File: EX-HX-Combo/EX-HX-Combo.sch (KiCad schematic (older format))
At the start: 39 parts, among them CN1 DB9 Male, J1 IDE_CONNECTOR, J200 Bus_Tandy_Plus_Through, J3 Bus_Tandy_Plus, SW1 SW_DIP_x10, U1 BIOS FLASH, U2 74HCT245, U3 1.8432 MHz, U4 DS1315, U5 AS6C4008-55PCN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

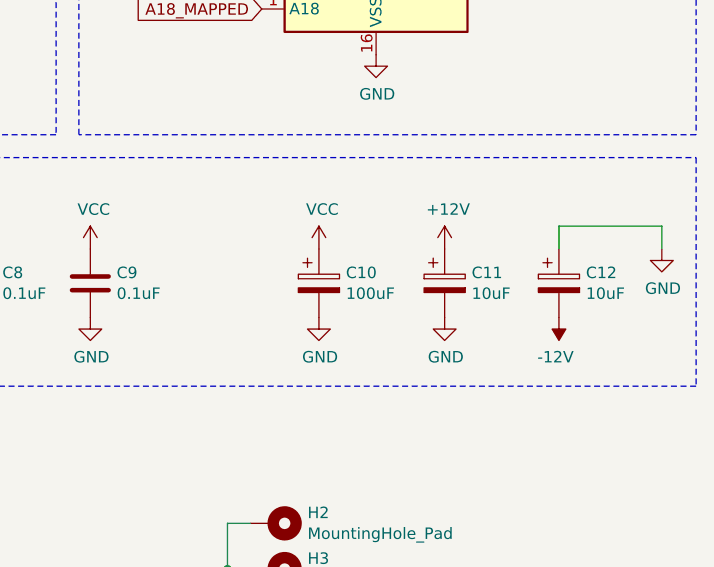
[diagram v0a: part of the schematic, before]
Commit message: More WIP on redo of through hole layout for EX-HX Combo.
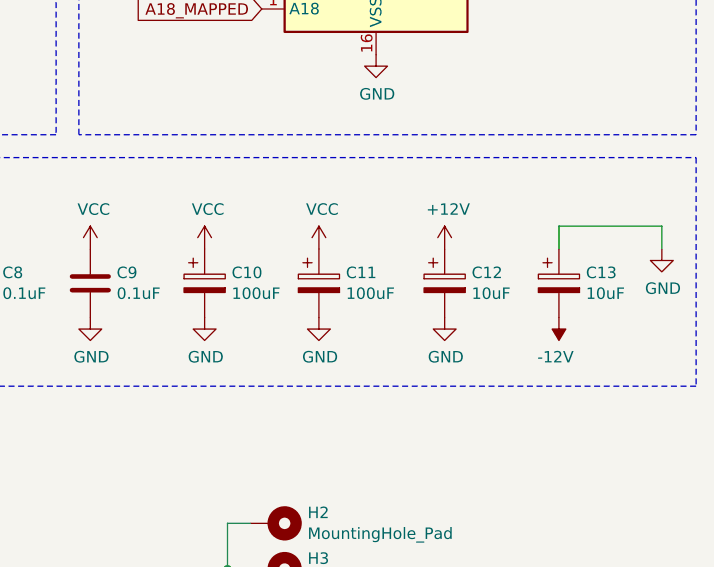
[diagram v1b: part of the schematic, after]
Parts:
- added C10: 100uF, Capacitor_Tantalum_SMD:CP_EIA-3528-15_AVX-H, symbol Device:CP
- C12: renamed from C11; footprint Capacitor_Tantalum_SMD:CP_EIA-3216-18_Kemet-A -> Capacitor_Tantalum_SMD:CP_EIA-3528-15_AVX-H
- C13: renamed from C12; footprint Capacitor_Tantalum_SMD:CP_EIA-3216-18_Kemet-A -> Capacitor_Tantalum_SMD:CP_EIA-3528-15_AVX-H
- renumbered C10 to C11
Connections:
- net GND: now also C10.2
- net VCC: now also C10.1
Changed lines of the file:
@@
 UART_XIN
 $Comp
-L Device:CP C10
+L Device:CP C11
 U 1 1 60E3E53A
 P 13400 7700
-F 0 "C10" H 13518 7746 50  0000 L CNN
+F 0 "C11" H 13518 7746 50  0000 L CNN
 F 1 "100uF" H 13518 7655 50  0000 L CNN
 F 2 "Capacitor_Tantalum_SMD:CP_EIA-3528-15_AVX-H" H 13438 7550 50  0001 C CNN
@@
 $EndComp
 $Comp
-L Device:CP C11
+L Device:CP C12
 U 1 1 60D204F0
 P 13950 7700
-F 0 "C11" H 14068 7746 50  0000 L CNN
+F 0 "C12" H 14068 7746 50  0000 L CNN
 F 1 "10uF" H 14068 7655 50  0000 L CNN
-F 2 "Capacitor_Tantalum_SMD:CP_EIA-3216-18_Kemet-A" H 13988 7550 50  0001 C CNN
+F 2 "Capacitor_Tantalum_SMD:CP_EIA-3528-15_AVX-H" H 13988 7550 50  0001 C CNN
 F 3 "~" H 13950 7700 50  0001 C CNN
 	1    13950 7700
@@
 $EndComp
 $Comp
-L Device:CP C12
+L Device:CP C13
 U 1 1 60D20522
 P 14450 7700
-F 0 "C12" H 14568 7746 50  0000 L CNN
+F 0 "C13" H 14568 7746 50  0000 L CNN
 F 1 "10uF" H 14568 7655 50  0000 L CNN
-F 2 "Capacitor_Tantalum_SMD:CP_EIA-3216-18_Kemet-A" H 14488 7550 50  0001 C CNN
+F 2 "Capacitor_Tantalum_SMD:CP_EIA-3528-15_AVX-H" H 14488 7550 50  0001 C CNN
 F 3 "~" H 14450 7700 50  0001 C CNN
 	1    14450 7700
@@
 Text GLabel 11100 2300 2    50   Input ~ 0
 D2_BUF
+$Comp
+L power:VCC #PWR0171
+U 1 1 6117F173
+P 12900 7550
+F 0 "#PWR0171" H 12900 7400 50  0001 C CNN
+F 1 "VCC" H 12915 7723 50  0000 C CNN
+F 2 "" H 12900 7550 50  0001 C CNN
+F 3 "" H 12900 7550 50  0001 C CNN
+	1    12900 7550
+	1    0    0    -1
+$EndComp
+$Comp
+L power:GND #PWR0172
+U 1 1 6117FB7B
+P 12900 7850
+F 0 "#PWR0172" H 12900 7600 50  0001 C CNN
+F 1 "GND" H 12905 7677 50  0000 C CNN
+F 2 "" H 12900 7850 50  0001 C CNN
+F 3 "" H 12900 7850 50  0001 C CNN
+	1    12900 7850
+	1    0    0    -1
+$EndComp
+$Comp
+L Device:CP C10
+U 1 1 6117FB85
+P 12900 7700
+F 0 "C10" H 13018 7746 50  0000 L CNN
+F 1 "100uF" H 13018 7655 50  0000 L CNN
+F 2 "Capacitor_Tantalum_SMD:CP_EIA-3528-15_AVX-H" H 12938 7550 50  0001 C CNN
+F 3 "~" H 12900 7700 50  0001 C CNN
+	1    12900 7700
+	1    0    0    -1
+$EndComp
 $EndSCHEMATC

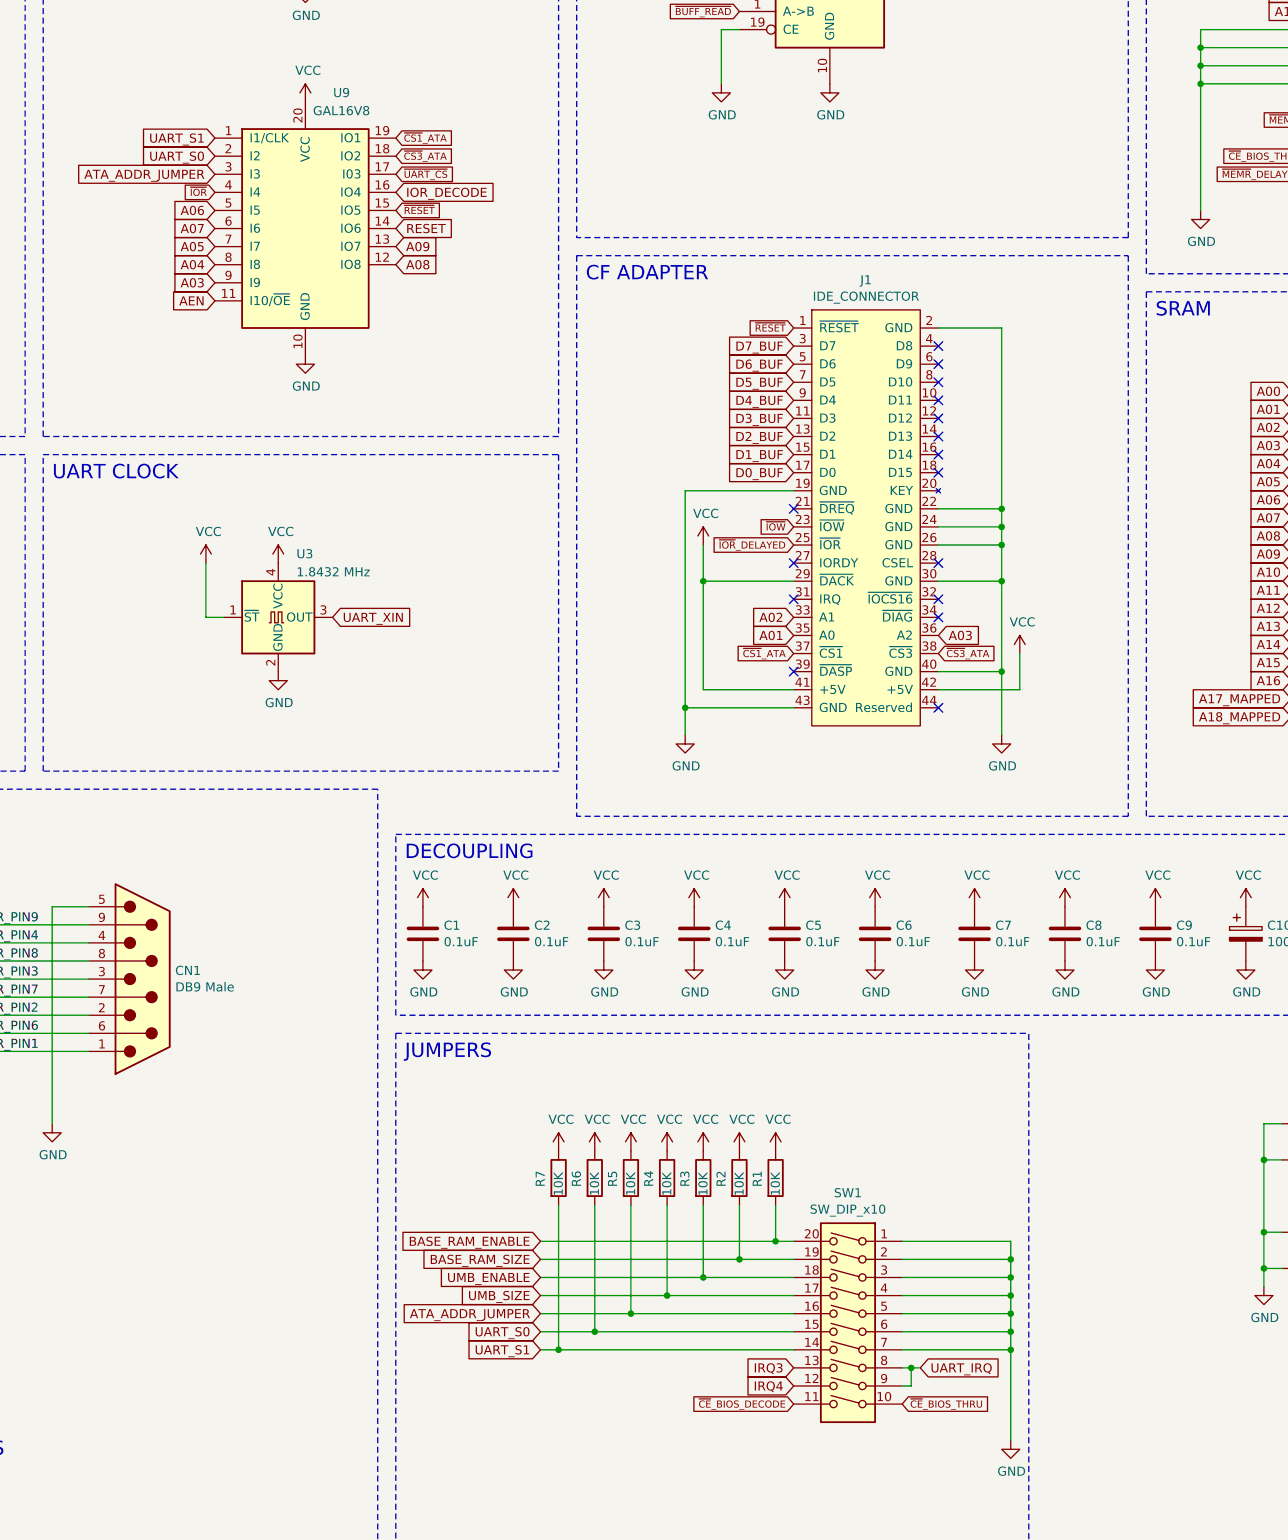
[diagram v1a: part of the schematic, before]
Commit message: More layout work on EX-HX combo.
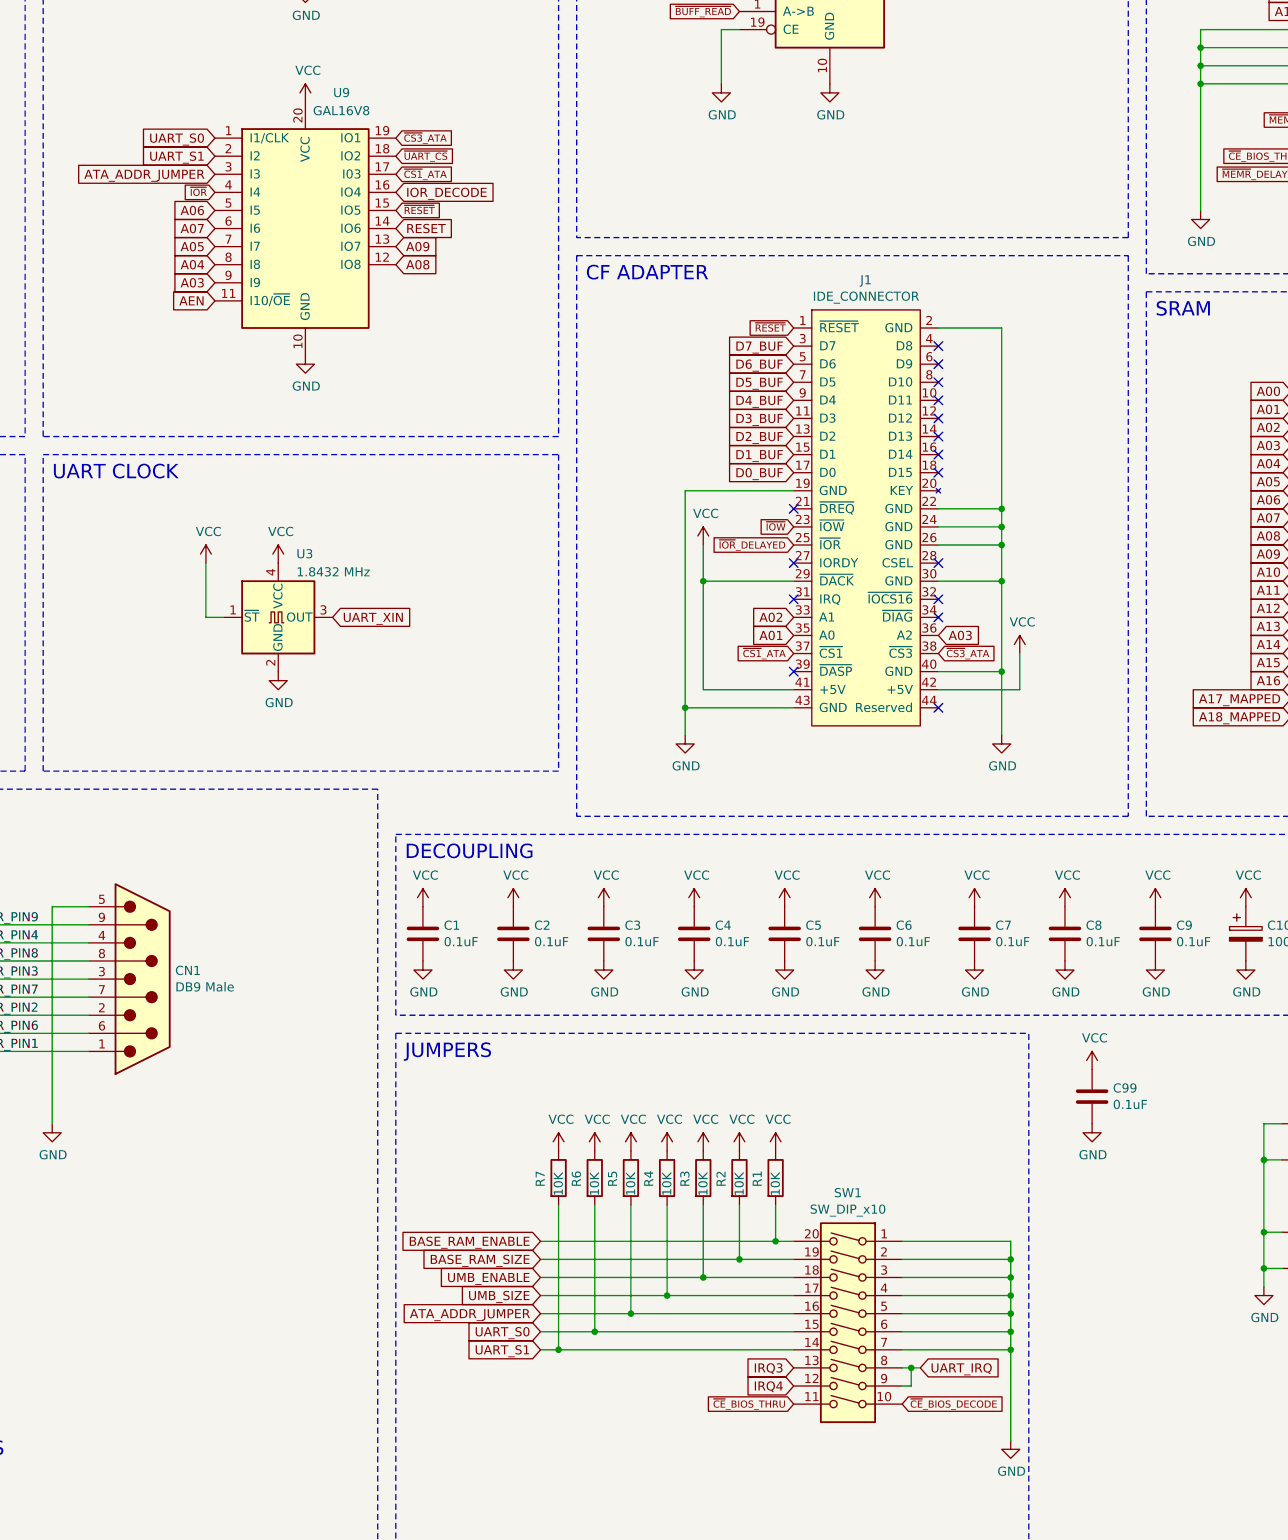
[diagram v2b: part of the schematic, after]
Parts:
- added C99: 0.1uF, Capacitor_SMD:C_1206_3216Metric, symbol Device:C
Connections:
- net GND: now also C99.2
- net UART_S0: now also U9.1 (I1/CLK); no longer U9.2 (I2)
- net UART_S1: now also U9.2 (I2); no longer U9.1 (I1/CLK)
- net VCC: now also C99.1
- net ~CE~_BIOS_DECODE: now also SW1.10; no longer SW1.11
- net ~CE~_BIOS_THRU: now also SW1.11; no longer SW1.10
- net ~CS1~_ATA: now also U9.17 (I03); no longer U9.19 (IO1)
- net ~CS3~_ATA: now also U9.19 (IO1); no longer U9.18 (IO2)
- net ~UART_CS: now also U9.18 (IO2); no longer U9.17 (I03)
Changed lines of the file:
@@
 Text GLabel 8200 1950 2    50   Input ~ 0
 A15
-Text GLabel 7200 3300 0    50   Input ~ 0
+Text GLabel 7200 3400 0    50   Input ~ 0
 UART_S1
-Text GLabel 8200 3300 2    39   Input ~ 0
+Text GLabel 8200 3500 2    39   Input ~ 0
 ~CS1~_ATA
-Text GLabel 8200 3500 2    39   Input ~ 0
+Text GLabel 8200 3400 2    39   Input ~ 0
 ~UART_CS
 Text GLabel 8200 1350 2    39   Input ~ 0
@@
 Wire Notes Line
 	12250 3950 12250 7050
-Text GLabel 8200 3400 2    39   Input ~ 0
+Text GLabel 8200 3300 2    39   Input ~ 0
 ~CS3~_ATA
 Text GLabel 11200 6150 2    39   Input ~ 0
 ~CS3~_ATA
-Text GLabel 7200 3400 0    50   Input ~ 0
+Text GLabel 7200 3300 0    50   Input ~ 0
 UART_S0
 Text GLabel 8200 3800 2    50   Input ~ 0
@@
 	-1   0    0    -1
 $EndComp
+Text GLabel 11000 10300 2    39   Input ~ 0
+~CE~_BIOS_DECODE
 Text GLabel 10400 10300 0    39   Input ~ 0
-~CE~_BIOS_DECODE
-Text GLabel 11000 10300 2    39   Input ~ 0
 ~CE~_BIOS_THRU
 Wire Wire Line
@@
 	1    0    0    -1
 $EndComp
+$Comp
+L Device:C C99
+U 1 1 6131AD4C
+P 12050 8600
+F 0 "C99" H 12165 8646 50  0000 L CNN
+F 1 "0.1uF" H 12165 8555 50  0000 L CNN
+F 2 "Capacitor_SMD:C_1206_3216Metric" H 12088 8450 50  0001 C CNN
+F 3 "~" H 12050 8600 50  0001 C CNN
+	1    12050 8600
+	1    0    0    -1
+$EndComp
+$Comp
+L power:GND #PWR0173
+U 1 1 6131B788
+P 12050 8750
+F 0 "#PWR0173" H 12050 8500 50  0001 C CNN
+F 1 "GND" H 12055 8577 50  0000 C CNN
+F 2 "" H 12050 8750 50  0001 C CNN
+F 3 "" H 12050 8750 50  0001 C CNN
+	1    12050 8750
+	1    0    0    -1
+$EndComp
+$Comp
+L power:VCC #PWR0174
+U 1 1 6131B792
+P 12050 8450
+F 0 "#PWR0174" H 12050 8300 50  0001 C CNN
+F 1 "VCC" H 12065 8623 50  0000 C CNN
+F 2 "" H 12050 8450 50  0001 C CNN
+F 3 "" H 12050 8450 50  0001 C CNN
+	1    12050 8450
+	1    0    0    -1
+$EndComp

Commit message: WIP on EX-HX-Combo layout - left side of board.
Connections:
- net A03: now also U9.5 (I5); no longer U9.9 (I9)
- net A04: now also U9.6 (I6); no longer U9.8 (I8)
- net A05: now also U9.8 (I8); no longer U9.7 (I7)
- net A06: now also U9.12 (IO8); no longer U9.5 (I5)
- net A07: now also U9.11 (I10/~OE~); no longer U9.6 (I6)
- net A08: now also U9.13 (IO7); no longer U9.12 (IO8)
- net A09: now also U9.14 (IO6); no longer U9.13 (IO7)
- net A15: now also U8.11 (I10/~OE~); no longer U8.12 (IO8)
- net A16: now also U8.6 (I6); no longer U8.7 (I7)
- net A17: now also U8.7 (I7); no longer U8.8 (I8)
- net A17_MAPPED: now also U8.15 (IO5); no longer U8.16 (IO4)
- net A18: now also U8.8 (I8); no longer U8.9 (I9)
- net A19: now also U8.9 (I9); no longer U8.11 (I10/~OE~)
- net AEN: now also U9.9 (I9); no longer U9.11 (I10/~OE~)
- net ATA_ADDR_JUMPER: now also U9.7 (I7); no longer U9.3 (I3)
- net IOR_DECODE: now also U8.4 (I4), U9.17 (I03); no longer U8.5 (I5), U9.16 (IO4)
- net RESET: now also U9.4 (I4); no longer U9.14 (IO6)
- net UMB_ENABLE: now also U8.5 (I5); no longer U8.3 (I3)
- net UMB_SIZE: now also U8.12 (IO8); no longer U8.6 (I6)
- net ~BUFF_READ: now also U8.16 (IO4); no longer U8.13 (IO7)
- net ~CS1~_ATA: now also U9.15 (IO5); no longer U9.17 (I03)
- net ~CS3~_ATA: now also U9.18 (IO2); no longer U9.19 (IO1)
- net ~IOR: now also U9.3 (I3); no longer U9.4 (I4)
- net ~IOR~_DELAYED: now also U8.13 (IO7); no longer U8.14 (IO6)
- net ~MEMR: now also U8.3 (I3); no longer U8.4 (I4)
- net ~MEMR~_DELAYED: now also U8.14 (IO6); no longer U8.15 (IO5)
- net ~RESET: now also U9.16 (IO4); no longer U9.15 (IO5)
- net ~UART_CS: now also U9.19 (IO1); no longer U9.18 (IO2)
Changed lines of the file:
@@
 Text GLabel 14450 1900 2    50   Input ~ 0
 D7_BUF
-Text GLabel 8200 1750 2    39   Input ~ 0
+Text GLabel 8200 1850 2    39   Input ~ 0
 ~IOR~_DELAYED
 Text GLabel 2700 3650 2    50   Input ~ 0
@@
 Text GLabel 10100 2600 0    39   Input ~ 0
 ~BUFF_READ
-Text GLabel 7200 3500 0    50   Input ~ 0
+Text GLabel 7200 3900 0    50   Input ~ 0
 ATA_ADDR_JUMPER
 Text GLabel 2700 2850 2    50   Input ~ 0
@@
 Wire Wire Line
 	2600 2850 2700 2850
-Text GLabel 7200 1550 0    39   Input ~ 0
+Text GLabel 7200 1450 0    39   Input ~ 0
 ~MEMR
 $Comp
@@
 	1    0    0    -1
 $EndComp
-Text GLabel 8200 1850 2    39   Input ~ 0
+Text GLabel 8200 1550 2    39   Input ~ 0
 ~BUFF_READ
-Text GLabel 7200 3600 0    39   Input ~ 0
+Text GLabel 7200 3500 0    39   Input ~ 0
 ~IOR
 Wire Notes Line
@@
 Wire Notes Line
 	15050 600  15050 4050
-Text GLabel 8200 1650 2    39   Input ~ 0
+Text GLabel 8200 1750 2    39   Input ~ 0
 ~MEMR~_DELAYED
 $Comp
@@
 	1    0    0    -1
 $EndComp
+Text GLabel 7200 2050 0    50   Input ~ 0
+A19
+Text GLabel 7200 1950 0    50   Input ~ 0
+A18
+Text GLabel 7200 1850 0    50   Input ~ 0
+A17
+Text GLabel 7200 1750 0    50   Input ~ 0
+A16
 Text GLabel 7200 2150 0    50   Input ~ 0
-A19
-Text GLabel 7200 2050 0    50   Input ~ 0
-A18
-Text GLabel 7200 1950 0    50   Input ~ 0
-A17
-Text GLabel 7200 1850 0    50   Input ~ 0
-A16
-Text GLabel 8200 1950 2    50   Input ~ 0
 A15
 Text GLabel 7200 3400 0    50   Input ~ 0
 UART_S1
-Text GLabel 8200 3500 2    39   Input ~ 0
+Text GLabel 8200 3700 2    39   Input ~ 0
 ~CS1~_ATA
-Text GLabel 8200 3400 2    39   Input ~ 0
+Text GLabel 8200 3300 2    39   Input ~ 0
 ~UART_CS
 Text GLabel 8200 1350 2    39   Input ~ 0
 ~CE~_RAM_DECODE
-Text GLabel 8200 1550 2    50   Input ~ 0
+Text GLabel 8200 1650 2    50   Input ~ 0
 A17_MAPPED
-Text GLabel 8200 3600 2    50   Input ~ 0
+Text GLabel 8200 3500 2    50   Input ~ 0
 IOR_DECODE
 Text GLabel 8200 1250 2    39   Input ~ 0
@@
 Text GLabel 7200 1350 0    50   Input ~ 0
 BASE_RAM_SIZE
-Text GLabel 7200 1450 0    50   Input ~ 0
+Text GLabel 7200 1650 0    50   Input ~ 0
 UMB_ENABLE
-Text GLabel 7200 1750 0    50   Input ~ 0
+Text GLabel 8200 1950 2    50   Input ~ 0
 UMB_SIZE
 $Comp
@@
 Wire Wire Line
 	1250 1850 1250 4450
-Text GLabel 7200 4200 0    50   Input ~ 0
+Text GLabel 7200 4100 0    50   Input ~ 0
 AEN
 Text GLabel 13150 6500 0    50   Input ~ 0
@@
 Wire Notes Line
 	12250 3950 12250 7050
-Text GLabel 8200 3300 2    39   Input ~ 0
+Text GLabel 8200 3400 2    39   Input ~ 0
 ~CS3~_ATA
 Text GLabel 11200 6150 2    39   Input ~ 0
@@
 Text GLabel 7200 3300 0    50   Input ~ 0
 UART_S0
-Text GLabel 8200 3800 2    50   Input ~ 0
+Text GLabel 7200 3600 0    50   Input ~ 0
 RESET
-Text GLabel 8200 3700 2    39   Input ~ 0
+Text GLabel 8200 3600 2    39   Input ~ 0
 ~RESET
-Text GLabel 7200 1650 0    50   Input ~ 0
+Text GLabel 7200 1550 0    50   Input ~ 0
 IOR_DECODE
 Text GLabel 1350 10150 0    50   Input ~ 0
@@
 Text GLabel 10400 5150 0    50   Input ~ 0
 D0_BUF
-Text GLabel 7200 4100 0    50   Input ~ 0
+Text GLabel 7200 3700 0    50   Input ~ 0
 A03
+Text GLabel 7200 3800 0    50   Input ~ 0
+A04
 Text GLabel 7200 4000 0    50   Input ~ 0
-A04
-Text GLabel 7200 3900 0    50   Input ~ 0
 A05
-Text GLabel 7200 3700 0    50   Input ~ 0
+Text GLabel 8200 4000 2    50   Input ~ 0
 A06
+Text GLabel 8200 3800 2    50   Input ~ 0
+A09
 Text GLabel 8200 3900 2    50   Input ~ 0
-A09
-Text GLabel 8200 4000 2    50   Input ~ 0
 A08
-Text GLabel 7200 3800 0    50   Input ~ 0
+Text GLabel 7200 4200 0    50   Input ~ 0
 A07
 Text GLabel 9000 9700 0    50   Input ~ 0
